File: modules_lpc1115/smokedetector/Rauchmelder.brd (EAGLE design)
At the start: 38 x 65 mm, 75 parts, among them IC1 BD9G101, IC2 LPC1115, Q1 BC856, Q3 BCP52, Q4 ASFL, T1 BC847C, T2 BC817

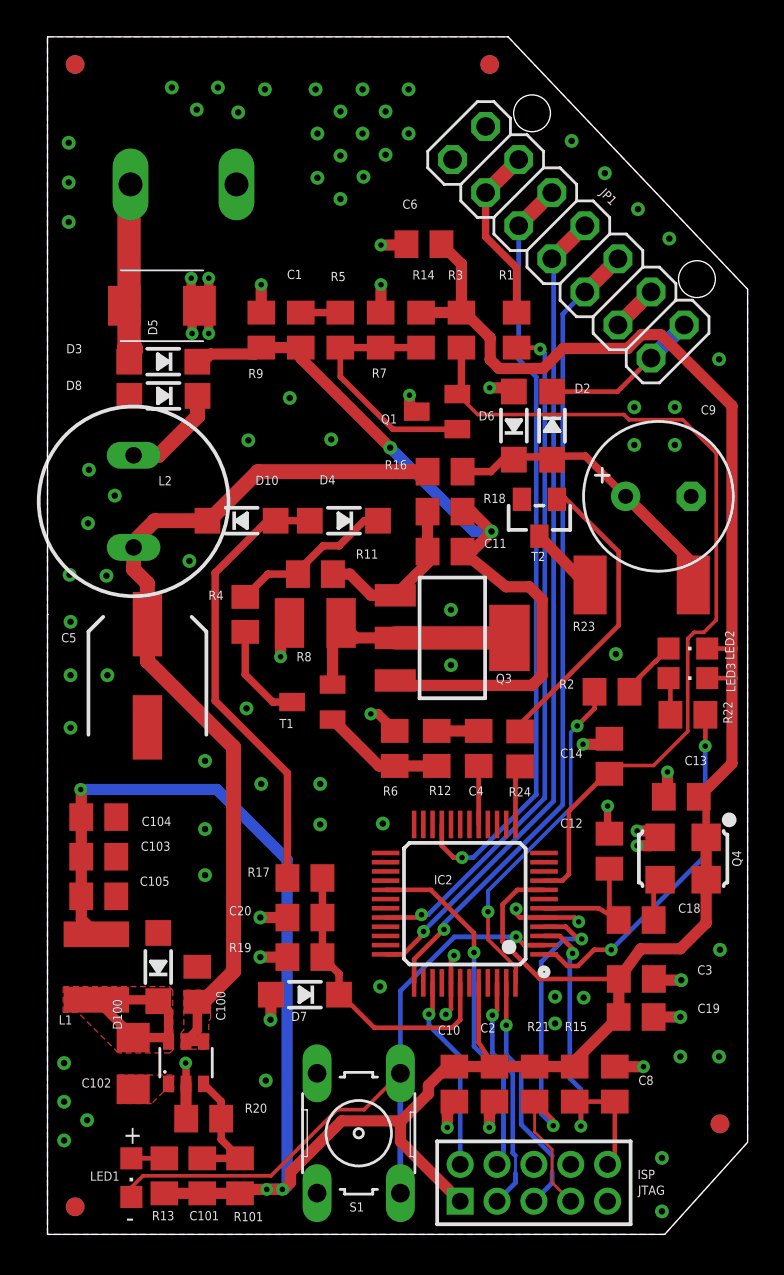
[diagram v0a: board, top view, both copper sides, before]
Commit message: [RM] - corrected some small bugs
corrected directions of status LEDs 
changed C102 1206 -> 0805
changed L1 6.8uH -> 4.7uH
changed C101 270 -> 470nF
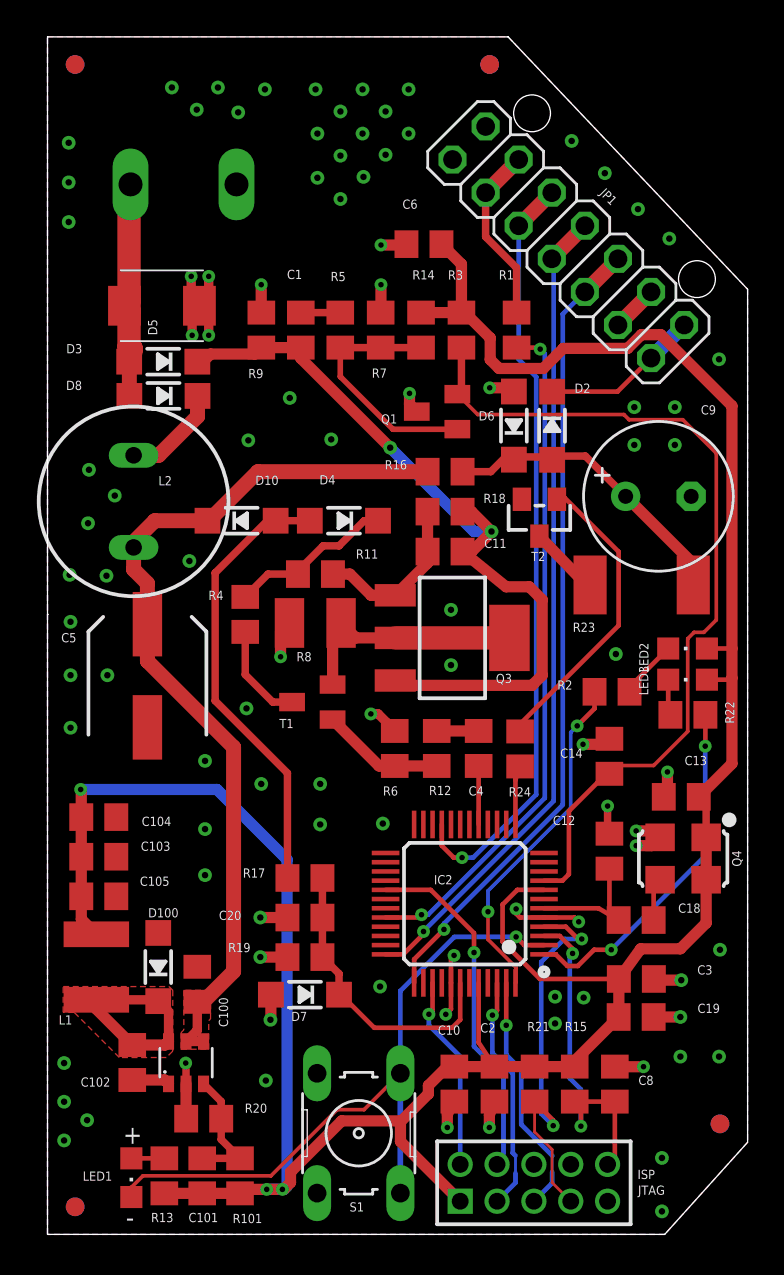
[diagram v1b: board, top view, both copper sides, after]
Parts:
- C102: device rcl:C1206 -> rcl:R0805
- moved LED3 0.08 mm to (34.7, 30.1), turned to 90 degrees
- moved C102 0.07 mm to (4.60, 9.33)
- turned LED2 to 90 degrees
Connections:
- net +3V3: now also LED2.A, LED3.A; no longer LED2.C, LED3.C
- net N$3: now also LED3.C, R22.2; no longer LED2.A, R2.2
- net N$5: now also LED2.C, R2.2; no longer LED3.A, R22.2
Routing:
- net BST: track 0.00 -> 2.06 mm
- net EIB+: track 9.92 -> 11.8 mm
- net N$3: track 3.24 -> 1.96 mm
- net N$5: track 2.03 -> 3.22 mm
- net GND: track 49.3 -> 49.9 mm
- removed copper zone on layer 1, net BST
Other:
- board text added: "Selfbus RM-ARM v3.8.4 RC1"
- board text removed: "Selfbus RM-ARM v3.8.3 beta1"

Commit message: [RM] - corrected some small bugs - 2nd try
something went wrong yesterday - now again: 
corrected directions of status LEDs 
changed C102 1206 -> 0805
changed L1 6.8uH -> 4.7uH
changed C101 270 -> 470nF
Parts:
- C101: value 270nF -> 470nF
- L1: value 6.8uH -> 4.7uH
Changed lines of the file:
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@@
 <attribute name="VALUE" x="9.372" y="9.598" size="0.5" layer="27" ratio="10"/>
 </element>
-<element name="L1" library="rcl_changed" package="L4532P" package3d_urn="urn:adsk.eagle:package:23484/1" value="6.8uH" x="2.65" y="14.5113" smashed="yes" rot="R90">
+<element name="L1" library="rcl_changed" package="L4532P" package3d_urn="urn:adsk.eagle:package:23484/1" value="4.7uH" x="2.65" y="14.5113" smashed="yes" rot="R90">
 <attribute name="NAME" x="0.6063" y="11.39" size="0.5" layer="25"/>
 <attribute name="POPULARITY" value="0" x="2.65" y="14.5113" size="1.778" layer="27" rot="R90" display="off"/>
@@
 <attribute name="VALUE" x="10.707" y="5.89" size="0.5" layer="27"/>
 </element>
-<element name="C101" library="rcl" library_urn="urn:adsk.eagle:library:334" package="C0805" package3d_urn="urn:adsk.eagle:package:23617/2" value="270nF" x="8.396" y="3.1774125" smashed="yes" rot="R270">
+<element name="C101" library="rcl" library_urn="urn:adsk.eagle:library:334" package="C0805" package3d_urn="urn:adsk.eagle:package:23617/2" value="470nF" x="8.396" y="3.1774125" smashed="yes" rot="R270">
 <attribute name="NAME" x="7.6525875" y="0.666" size="0.5" layer="25"/>
 <attribute name="POPULARITY" value="88" x="8.396" y="3.1774125" size="1.778" layer="27" rot="R270" display="off"/>
